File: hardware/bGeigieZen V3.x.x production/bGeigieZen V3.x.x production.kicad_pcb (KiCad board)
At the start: 2 copper layers, 129.4 x 64.6 mm, 16 parts, among them J1 M5 2x15 pin, J10 QI GND, J11 QI charger Plus, J2 Geiger IRover, J3 GPS, J4 Geiger Safepulse, J5 Extra support header, J6 Grove, J8 QI charger ground, J9 QI Plus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

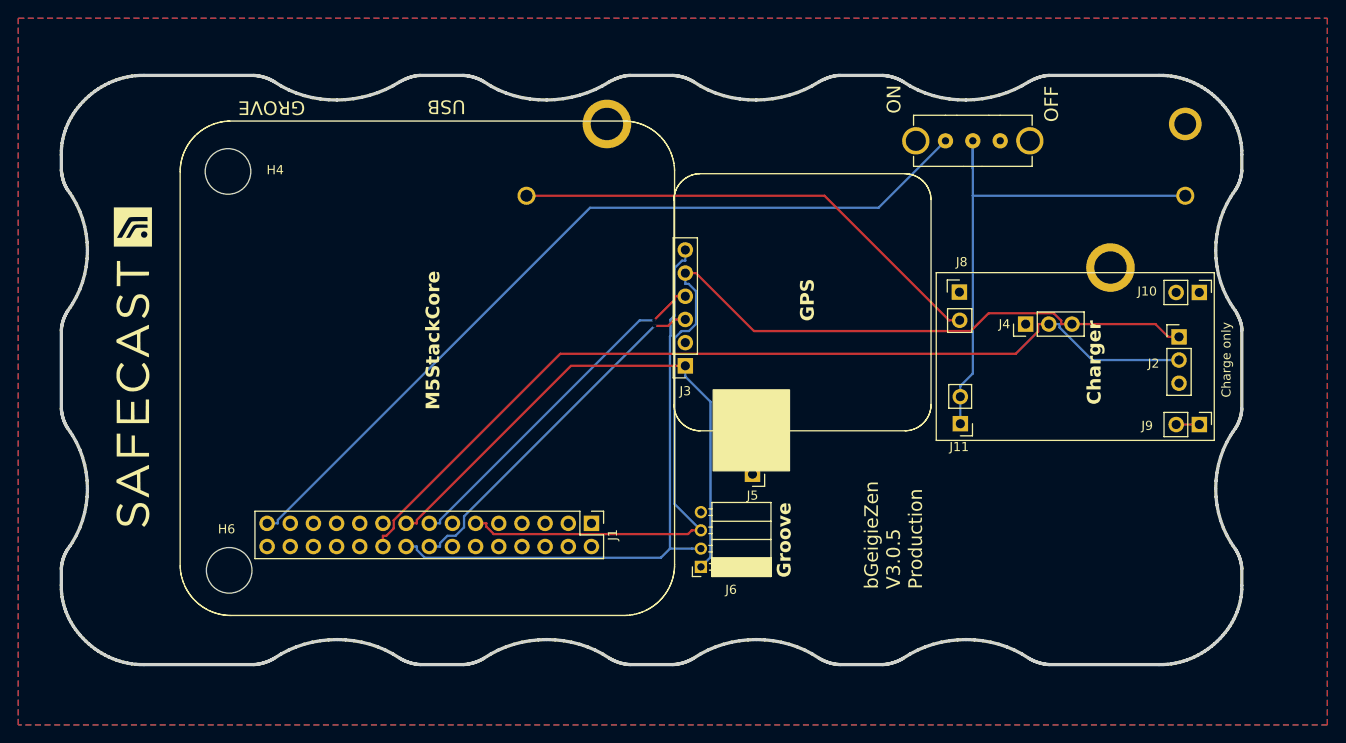
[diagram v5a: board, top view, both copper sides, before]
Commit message: Swapped SDA and SCL lines on GPS
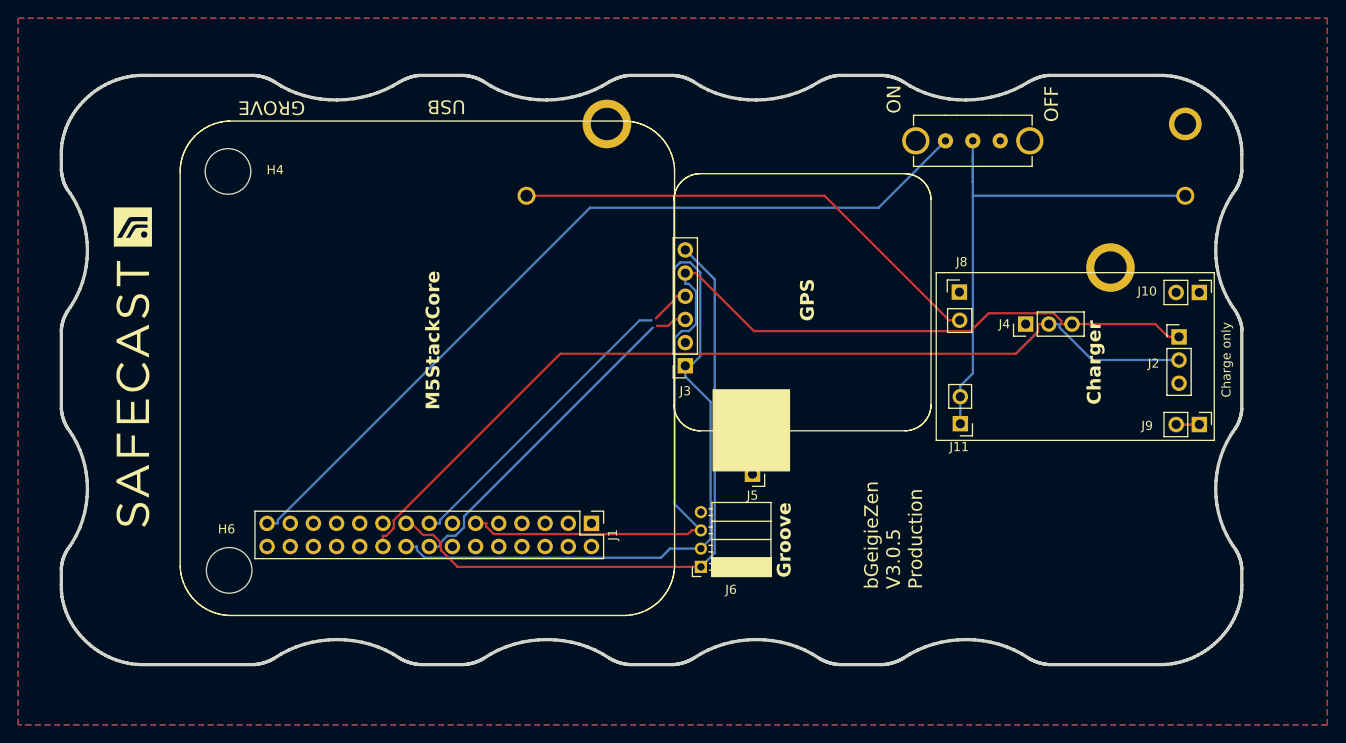
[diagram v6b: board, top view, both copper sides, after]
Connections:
- J3 pad 1: /SCL -> /SDA
- J3 pad 6: /SDA -> /SCL
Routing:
- net /SCL: track 61.6 -> 71.5 mm
- net /SDA: track 67.7 -> 70.3 mm
- net /VBATT: track 57.9 -> 57.1 mm

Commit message: Update Board V3.0.5
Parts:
- BT1: footprint bGeigieZen:1043 -> bGeigieZen:BATTERY_18650-HOLDER
- moved BT1 32.2 mm to (176.1, 73.9), turned to 180 degrees
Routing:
- net Net-(BT1--): track 53.1 -> 46.5 mm, vias 0 -> 1
- net /VBATT: track 57.1 -> 54.2 mm

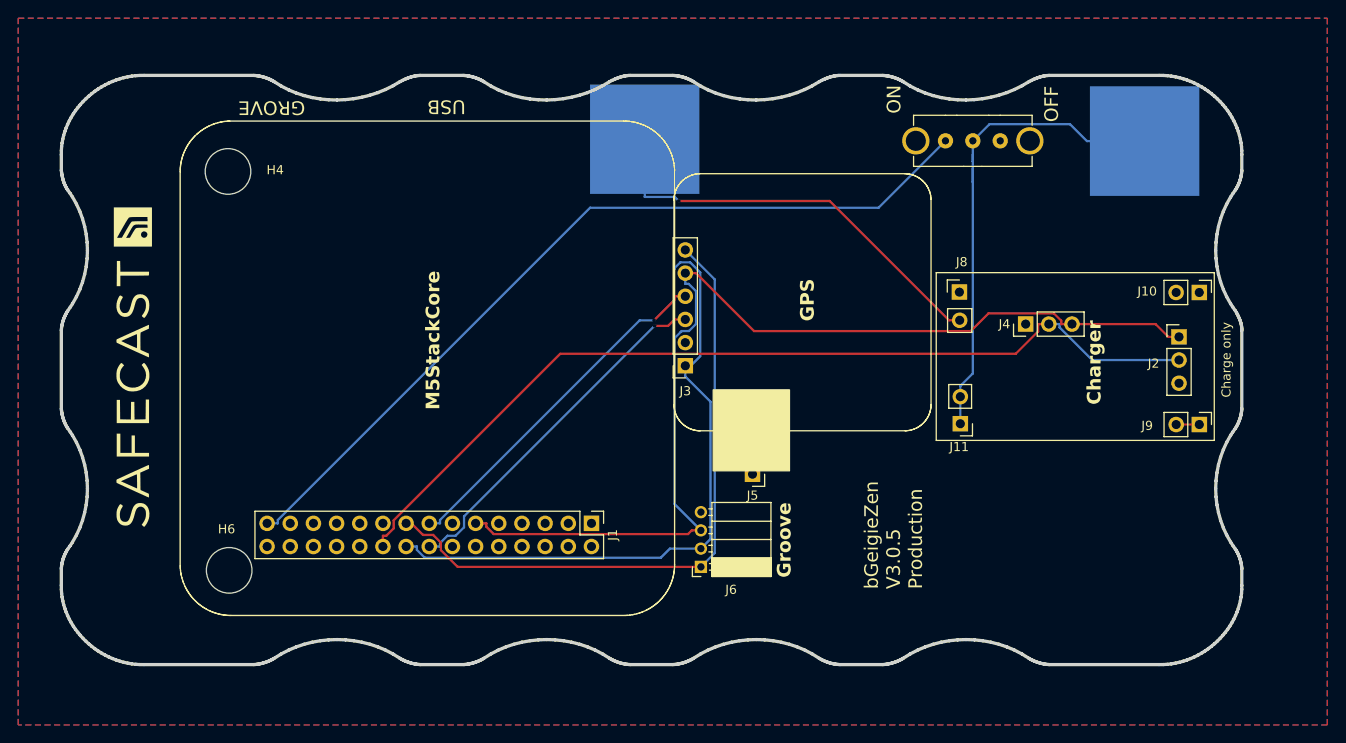
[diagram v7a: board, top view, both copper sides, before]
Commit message: Updated V3.0.5 boards with fixes for TP4056
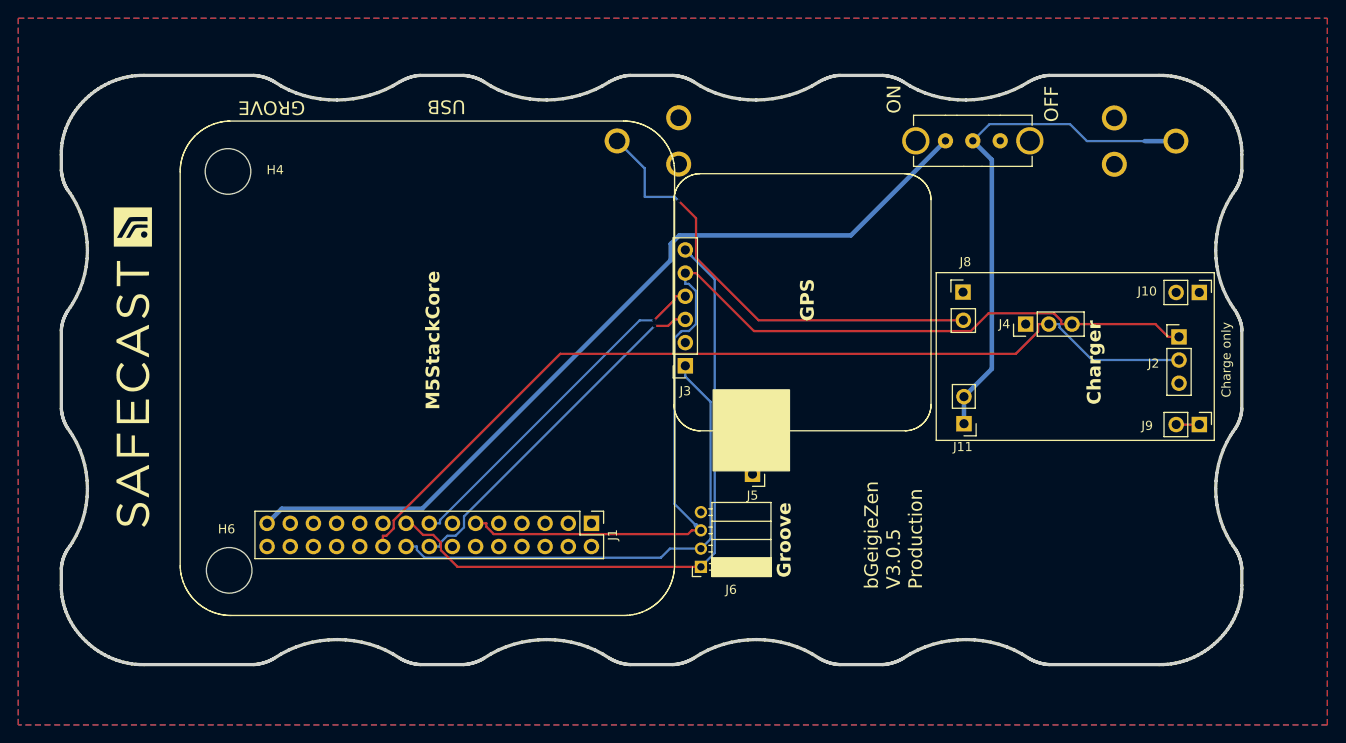
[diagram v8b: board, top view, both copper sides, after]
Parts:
- BT1: footprint bGeigieZen:BATTERY_18650-HOLDER -> bGeigieRaku_M5_1015:BATTERY_18650-HOLDER
- moved J11 0.40 mm to (183.5, 104.8)
- moved J8 0.40 mm to (183.4, 90.4)
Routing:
- net /SDA: track 70.5 -> 55.3 mm
- net Net-(BT1--): track 46.5 -> 50.5 mm
- net /VBATT: track 54.2 -> 56.9 mm
- net /SCL: track 71.5 -> 72.4 mm
- net /BAT: track 92.0 -> 92.8 mm
- net 3.3V: track 116.5 -> 117.2 mm
